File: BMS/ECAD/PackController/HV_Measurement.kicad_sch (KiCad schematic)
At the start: 52 parts, among them U901 ADCMP393ARZ, U906 LP5907MFX-3.3, U907 AMC0311R, U908 TEA1-0505HI, U909 LP5907MFX-3.3, U910 AMC0311R, U911 TEA1-0505HI

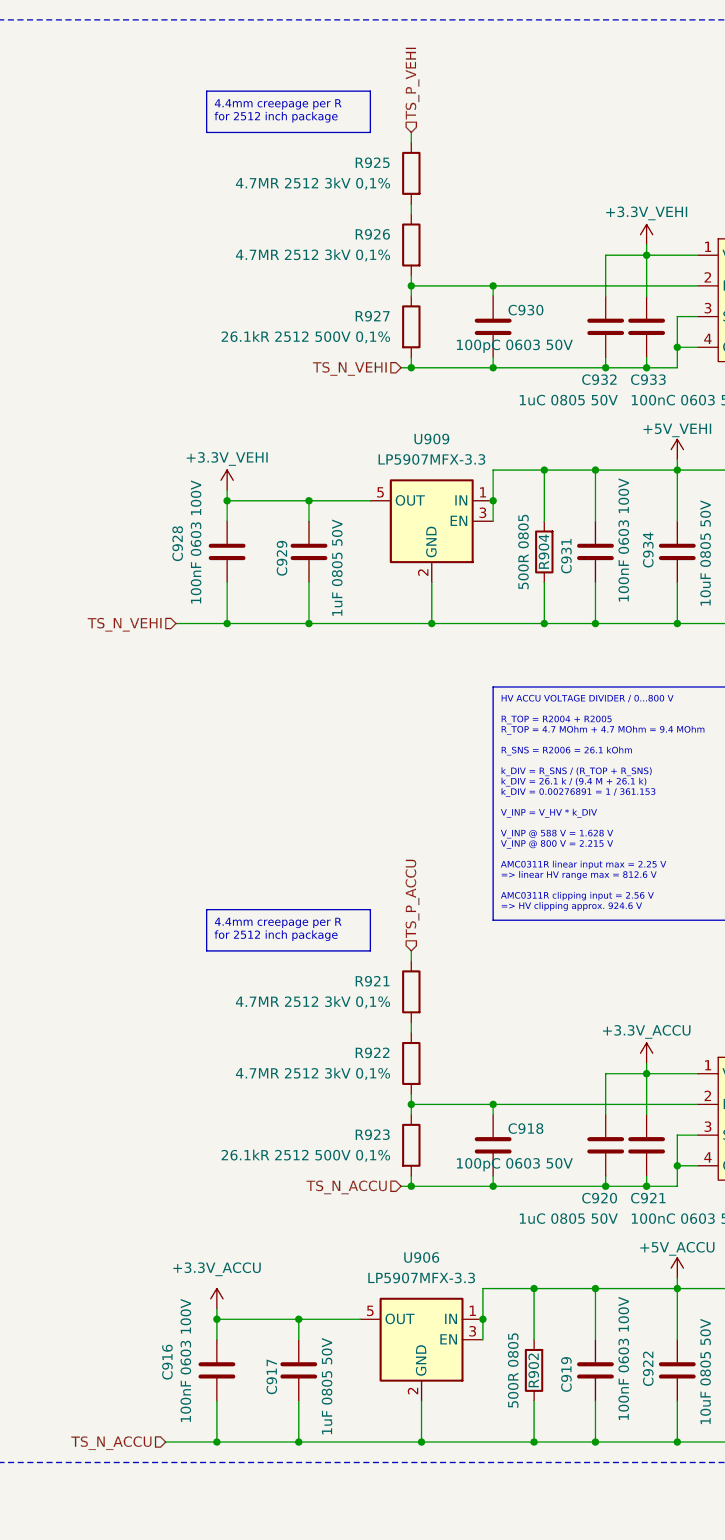
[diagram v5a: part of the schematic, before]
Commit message: add rule areas for hv separation
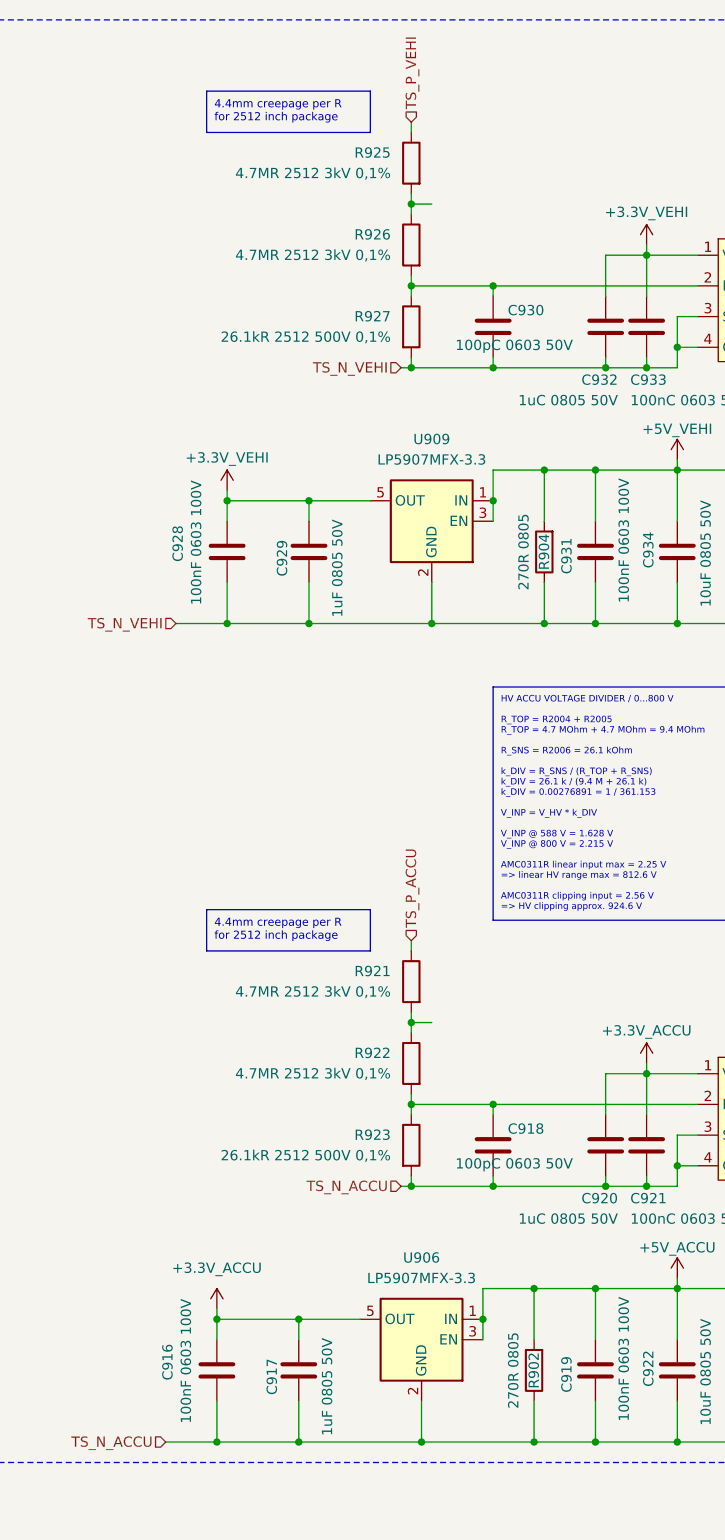
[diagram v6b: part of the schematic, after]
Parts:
- R902, R904: value 500R 0805 -> 270R 0805
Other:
- moved on the sheet: R921, R925

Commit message: yes
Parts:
- removed R908: 68,1K 0.1%, Resistor_SMD:R_0603_1608Metric_Pad0.98x0.95mm_HandSolder, symbol Device:R
- removed R910: 3.9k 0.1%, Resistor_SMD:R_0603_1608Metric_Pad0.98x0.95mm_HandSolder, symbol Device:R
- removed R915: 100kR 0.1%, Resistor_SMD:R_0603_1608Metric_Pad0.98x0.95mm_HandSolder, symbol Device:R
- removed R918, R919: 909kR 0.1%, Resistor_SMD:R_0603_1608Metric_Pad0.98x0.95mm_HandSolder, symbol Device:R
- added R905: 909kR 0.1%, Resistor_SMD:R_0603_1608Metric_Pad0.98x0.95mm_HandSolder, symbol Device:R
- C922, C923, C934: value 10uF 0805 50V -> 10uF 0805 35V
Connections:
- net GND: now also R905.2
- net at U901.5 (+): now also R901.2, R903.1, U901.6 (-)
- net at R917.2, U901.8 (-): now also U901.11 (+), R905.1
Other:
- moved on the sheet: R903, R909, R917, R920, U901A, U901D
